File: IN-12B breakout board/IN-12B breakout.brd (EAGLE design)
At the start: 30 x 32 mm, 25 parts, among them Q1 500mA/300V, Q10 500mA/300V, Q2 500mA/300V, Q3 500mA/300V, Q4 500mA/300V, Q5 500mA/300V, Q6 500mA/300V, Q7 500mA/300V, Q8 500mA/300V, Q9 500mA/300V

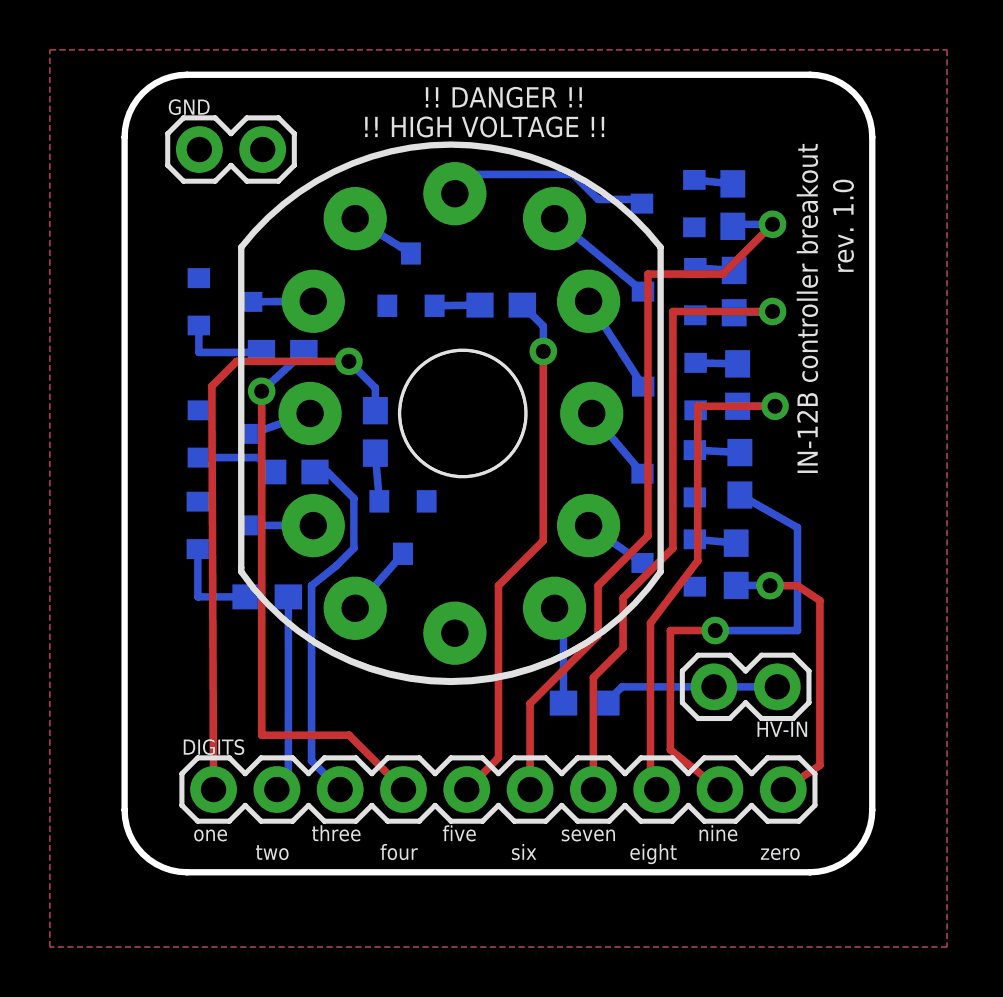
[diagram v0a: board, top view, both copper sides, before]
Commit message: board version 2.0, with decimal dot support
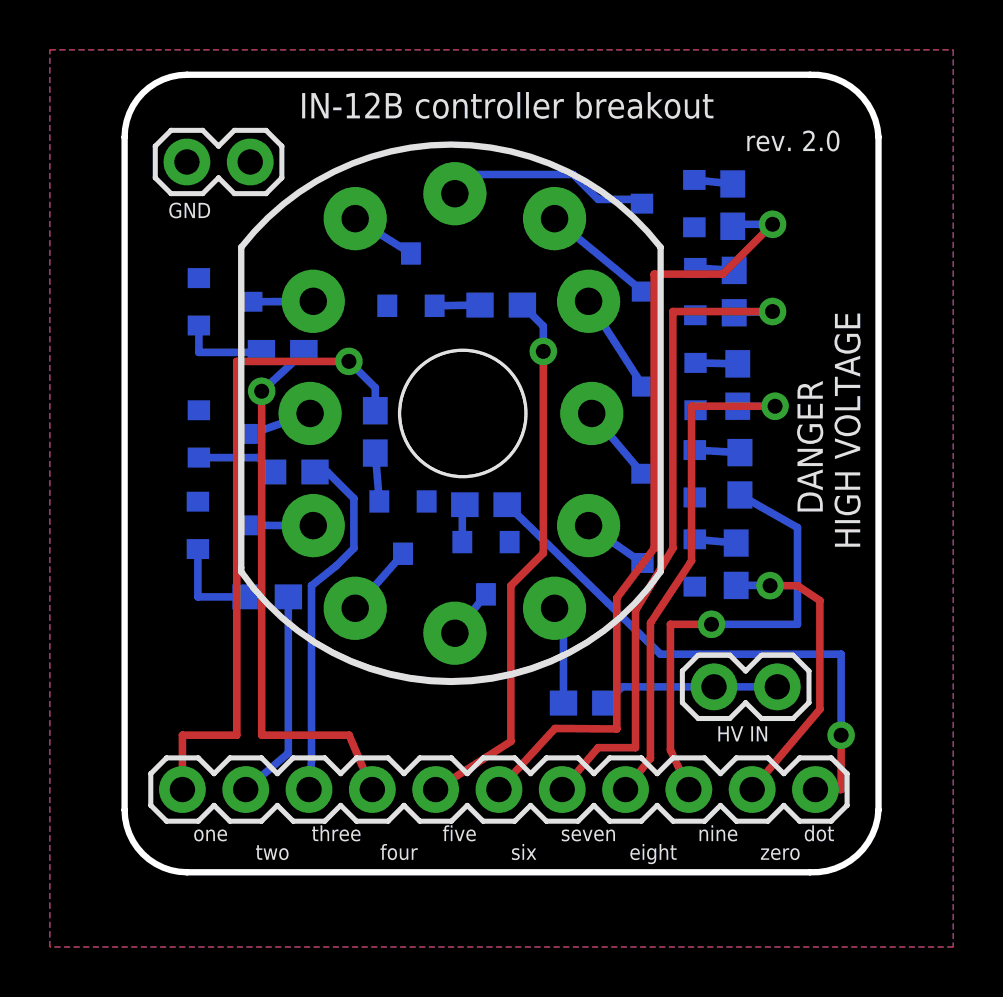
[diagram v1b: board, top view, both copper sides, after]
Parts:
- added Q11: 500mA/300V, SparkFun-DiscreteSemi:SOT23-3
- added R11: 33k, SparkFun-Resistors:0603
- DIGITS: device SparkFun-Connectors:1X10 -> SparkFun-Connectors:1X11
- moved DIGITS 1.25 mm to (2.32, 3.32)
- moved GND 0.71 mm to (2.50, 28.5)
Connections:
- new net DOT: DIGITS.11, R11.1
- new net LHDP: N1.LHDP, Q11.3
- new net N$22: Q11.1, R11.2
- net GND: now also Q11.2
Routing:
- net DOT: track 0.00 -> 22.3 mm, vias 0 -> 1
- net LHDP: track 0.00 -> 2.00 mm
- net ONE: track 24.5 -> 26.3 mm
- net SIX: track 30.1 -> 31.8 mm
- net N$22: track 0.00 -> 1.60 mm
- net SEVEN: track 26.0 -> 27.2 mm
- net FIVE: track 21.1 -> 22.0 mm
- net NINE: track 19.2 -> 18.4 mm
- net FOUR: track 22.7 -> 22.0 mm
- net TWO: track 7.92 -> 8.52 mm
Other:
- board size 30 x 32 mm -> 30.2 x 32 mm
- board text added: "DANGER"
- board text added: "GND"
- board text added: "HIGH VOLTAGE"
- board text added: "HV IN"
- board text added: "R CATH"
- board text added: "dot"
- board text added: "rev. 2.0"
- board text removed: "!! DANGER !!"
- board text removed: "!! HIGH VOLTAGE !!"
- board text removed: "rev. 1.0"

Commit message: BOM, CAD model
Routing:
- net DOT: track 22.3 -> 25.4 mm
- net FIVE: track 22.0 -> 22.6 mm, vias 1 -> 2
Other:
- board text added: "IN-12B Nixie controller breakout"
- board text added: "R."
- board text added: "R0"
- board text added: "R1"
- board text added: "R2"
- board text added: "R3"
- board text added: "R4"
- board text added: "R5"
- board text added: "R6"
- board text added: "R7"
- board text added: "R8"
- board text added: "R9"
- board text added: "T."
- board text added: "T0"
- board text added: "T1"
- board text added: "T2"
- board text added: "T3"
- board text added: "T4"
- board text added: "T5"
- board text added: "T6"
- board text added: "T7"
- board text added: "T8"
- board text added: "T9"
- board text added: "rev. 2.1"
- board text removed: "IN-12B controller breakout"
- board text removed: "rev. 2.0"
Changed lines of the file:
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@@
 <wire x1="0" y1="29.5" x2="0" y2="2.5" width="0.254" layer="20"/>
 <wire x1="0" y1="2.5" x2="2.5" y2="0" width="0.254" layer="20" curve="90"/>
-<text x="28.75" y="29.75" size="0.8128" layer="21" font="vector" rot="R180">rev. 2.0</text>
-<text x="7" y="30.25" size="1.016" layer="21" font="vector">IN-12B controller breakout</text>
-<text x="2.75" y="1.25" size="0.6096" layer="21" font="vector">one</text>
-<text x="5.25" y="0.5" size="0.6096" layer="21" font="vector">two</text>
-<text x="7.5" y="1.25" size="0.6096" layer="21" font="vector">three</text>
-<text x="10.25" y="0.5" size="0.6096" layer="21" font="vector">four</text>
-<text x="12.75" y="1.25" size="0.6096" layer="21" font="vector">five</text>
-<text x="15.5" y="0.5" size="0.6096" layer="21" font="vector">six</text>
-<text x="17.5" y="1.25" size="0.6096" layer="21" font="vector">seven</text>
-<text x="20.25" y="0.5" size="0.6096" layer="21" font="vector">eight</text>
-<text x="23" y="1.25" size="0.6096" layer="21" font="vector">nine</text>
-<text x="25.5" y="0.5" size="0.6096" layer="21" font="vector">zero</text>
-<text x="27.25" y="1.25" size="0.6096" layer="21" font="vector">dot</text>
+<text x="28.75" y="29.75" size="0.8128" layer="21" font="vector" rot="R180">rev. 2.1</text>
+<text x="1.75" y="30.25" size="1.016" layer="21" font="vector">IN-12B Nixie controller breakout</text>
+<text x="1.75" y="1.25" size="0.6096" layer="21" font="vector">one</text>
+<text x="4" y="0.75" size="0.6096" layer="21" font="vector">two</text>
+<text x="6.25" y="1.25" size="0.6096" layer="21" font="vector">three</text>
+<text x="9" y="0.75" size="0.6096" layer="21" font="vector">four</text>
+<text x="11.75" y="1.25" size="0.6096" layer="21" font="vector">five</text>
+<text x="14.25" y="0.75" size="0.6096" layer="21" font="vector">six</text>
+<text x="16" y="1.25" size="0.6096" layer="21" font="vector">seven</text>
+<text x="19" y="0.75" size="0.6096" layer="21" font="vector">eight</text>
+<text x="21.75" y="1.25" size="0.6096" layer="21" font="vector">nine</text>
+<text x="24" y="0.75" size="0.6096" layer="21" font="vector">zero</text>
+<text x="27" y="1.25" size="0.6096" layer="21" font="vector">dot</text>
 <text x="20" y="7.5" size="0.6096" layer="22" font="vector" rot="MR0">R CATH</text>
-<text x="1.75" y="26.25" size="0.6096" layer="21" font="vector">GND</text>
+<text x="3" y="26.25" size="0.6096" layer="21" font="vector">GND</text>
 <text x="23.75" y="5.25" size="0.6096" layer="21" font="vector">HV IN</text>
-<text x="27" y="19.75" size="1.016" layer="21" font="vector" rot="R270">DANGER</text>
-<text x="28.5" y="22.5" size="1.016" layer="21" font="vector" rot="R270">HIGH VOLTAGE</text>
+<text x="1.25" y="20.5" size="1.4224" layer="21" font="vector" rot="R270">DANGER</text>
+<text x="27.75" y="24.25" size="1.4224" layer="21" font="vector" rot="R270">HIGH VOLTAGE</text>
+<text x="4.25" y="24.5" size="0.4064" layer="22" font="vector" rot="MR0">T4</text>
+<text x="16.25" y="23.5" size="0.4064" layer="22" font="vector" rot="MR0">R5</text>
+<text x="6" y="21.5" size="0.4064" layer="22" font="vector" rot="MR0">R4</text>
+<text x="6.5" y="16.75" size="0.4064" layer="22" font="vector" rot="MR0">R3</text>
+<text x="10.75" y="19.5" size="0.4064" layer="22" font="vector" rot="MR0">R1</text>
+<text x="6" y="11.75" size="0.4064" layer="22" font="vector" rot="MR0">R2</text>
+<text x="25.75" y="27.75" size="0.4064" layer="22" font="vector" rot="MR0">R6</text>
+<text x="25.75" y="24.25" size="0.4064" layer="22" font="vector" rot="MR0">R7</text>
+<text x="26" y="20.5" size="0.4064" layer="22" font="vector" rot="MR0">R8</text>
+<text x="26" y="17" size="0.4064" layer="22" font="vector" rot="MR0">R9</text>
+<text x="26" y="13.25" size="0.4064" layer="22" font="vector" rot="MR0">R0</text>
+<text x="14.75" y="15.5" size="0.4064" layer="22" font="vector" rot="MR0">R.</text>
+<text x="21" y="17.5" size="0.4064" layer="22" font="vector" rot="MR0">T9</text>
+<text x="21" y="13.75" size="0.4064" layer="22" font="vector" rot="MR0">T0</text>
+<text x="21" y="21" size="0.4064" layer="22" font="vector" rot="MR0">T8</text>
+<text x="21" y="24.75" size="0.4064" layer="22" font="vector" rot="MR0">T7</text>
+<text x="21" y="28.25" size="0.4064" layer="22" font="vector" rot="MR0">T6</text>
+<text x="13" y="24.75" size="0.4064" layer="22" font="vector" rot="MR0">T5</text>
+<text x="4.25" y="19.25" size="0.4064" layer="22" font="vector" rot="MR0">T3</text>
+<text x="4.25" y="15.5" size="0.4064" layer="22" font="vector" rot="MR0">T2</text>
+<text x="11.5" y="14.75" size="0.4064" layer="22" font="vector" rot="MR0">T1</text>
+<text x="14.75" y="13.25" size="0.4064" layer="22" font="vector" rot="MR0">T.</text>
+<text x="29.25" y="20.75" size="1.4224" layer="22" font="vector" rot="MR270">DANGER</text>
+<text x="2.25" y="24.25" size="1.4224" layer="22" font="vector" rot="MR270">HIGH VOLTAGE</text>
 </plain>
 <attributes>
@@
 <contactref element="R5" pad="1"/>
 <contactref element="DIGITS" pad="5"/>
-<wire x1="16.8" y1="12.8" x2="16.8" y2="20.9" width="0.3048" layer="1"/>
-<via x="16.8" y="20.9" extent="1-16" drill="0.6" shape="octagon"/>
-<wire x1="16.8" y1="20.9" x2="16.8" y2="21.92" width="0.3048" layer="16"/>
-<wire x1="16.8" y1="21.92" x2="15.96" y2="22.76" width="0.3048" layer="16"/>
-<wire x1="16.8" y1="12.8" x2="15.5" y2="11.5" width="0.3048" layer="1"/>
-<wire x1="12.48" y1="3.32" x2="15.5" y2="5.25" width="0.3048" layer="1"/>
-<wire x1="15.5" y1="5.25" x2="15.5" y2="11.5" width="0.3048" layer="1"/>
+<via x="15.5" y="6.25" extent="1-16" drill="0.6" shape="octagon"/>
+<wire x1="15.5" y1="6.25" x2="15.5" y2="15" width="0.3048" layer="1"/>
+<wire x1="15.5" y1="15" x2="16.75" y2="16" width="0.3048" layer="1"/>
+<via x="16.75" y="16" extent="1-16" drill="0.6" shape="octagon"/>
+<wire x1="16.75" y1="16" x2="16.75" y2="22.01" width="0.3048" layer="16"/>
+<wire x1="16.75" y1="22.01" x2="15.96" y2="22.76" width="0.3048" layer="16"/>
+<wire x1="15.5" y1="6.25" x2="13.75" y2="6.25" width="0.254" layer="16"/>
+<wire x1="13.75" y1="6.25" x2="12.5" y2="5" width="0.254" layer="16"/>
+<wire x1="12.5" y1="5" x2="12.48" y2="3.32" width="0.254" layer="16"/>
 </signal>
 <signal name="SEVEN">
@@
 <contactref element="DIGITS" pad="11"/>
 <contactref element="R11" pad="1"/>
-<wire x1="15.35" y1="14.75" x2="21.5" y2="8.75" width="0.3048" layer="16"/>
 <via x="28.75" y="5.5" extent="1-16" drill="0.6" shape="octagon"/>
 <wire x1="28.75" y1="5.5" x2="28.75" y2="3.32" width="0.3048" layer="1"/>
 <wire x1="28.75" y1="3.32" x2="27.72" y2="3.32" width="0.3048" layer="1"/>
-<wire x1="21.5" y1="8.75" x2="28.75" y2="8.75" width="0.3048" layer="16"/>
+<wire x1="15.35" y1="14.75" x2="16.75" y2="14.75" width="0.3048" layer="16"/>
+<wire x1="16.75" y1="14.75" x2="16.75" y2="12.75" width="0.3048" layer="16"/>
+<wire x1="16.75" y1="12.75" x2="17.25" y2="12.25" width="0.3048" layer="16"/>
+<wire x1="17.25" y1="12.25" x2="18.75" y2="12.25" width="0.3048" layer="16"/>
+<wire x1="18.75" y1="12.25" x2="19" y2="12" width="0.3048" layer="16"/>
+<wire x1="19" y1="12" x2="19" y2="8.75" width="0.3048" layer="16"/>
+<wire x1="19" y1="8.75" x2="28.75" y2="8.75" width="0.3048" layer="16"/>
 <wire x1="28.75" y1="8.75" x2="28.75" y2="5.5" width="0.3048" layer="16"/>
 </signal>
